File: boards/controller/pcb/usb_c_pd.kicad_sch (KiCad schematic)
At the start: 17 parts, among them J5001 699C124-2A6-111, U5001 USBLC6-2SC6, U5002 TCPP01-M12, U5003 ISZ065N03L5SATMA1

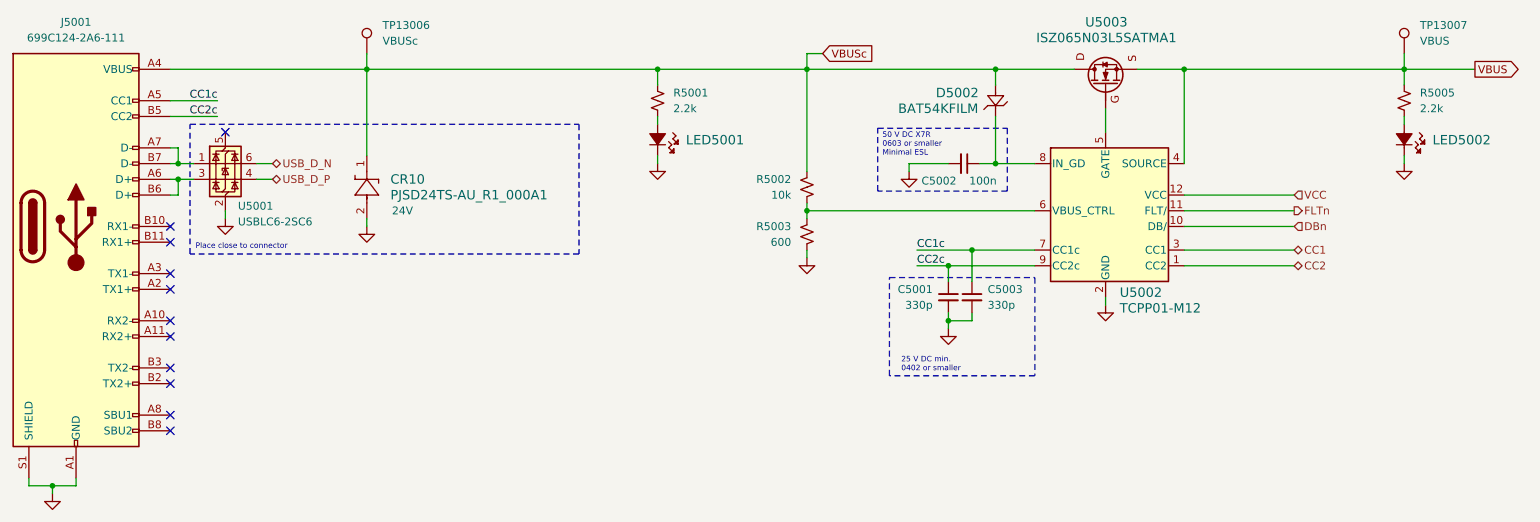
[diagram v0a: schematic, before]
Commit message: controller: pcb: Update schematic + layout
Signed-off-by: Nicholas Loehrke <nicholasnloehrke@gmail.com>
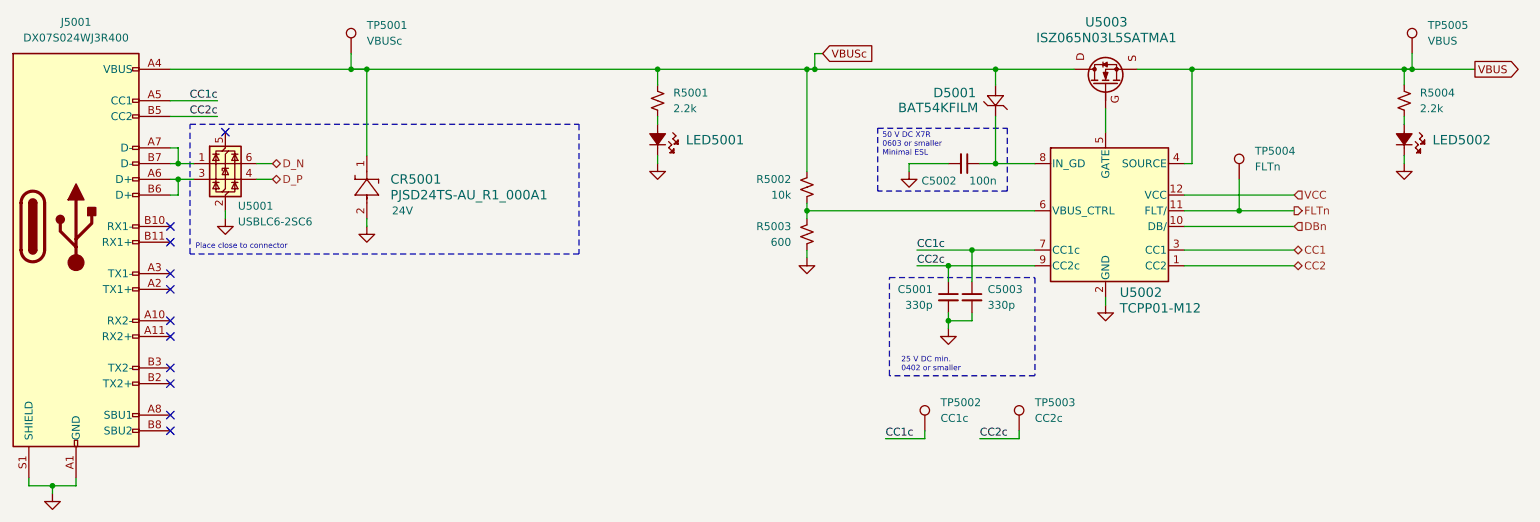
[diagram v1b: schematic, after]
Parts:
- removed D5002: BAT54KFILM, SOD-523_STM, symbol BAT54KFILM:BAT54KFILM
- removed J5001: 699C124-2A6-111, symbol Connector:USB_C_Receptacle
- added D5001: BAT54KFILM, BAT54KFILM:BAT54KFILM, symbol BAT54KFILM:BAT54KFILM
- added J5001: DX07S024WJ3R400, DX07S024WJ3R400:JAE_DX07S024WJ3R400, symbol DX07S024WJ3R400:DX07S024WJ3R400
- added TP5002: CC1c, TestPoint:TestPoint_Pad_D1.0mm, symbol Connector:TestPoint
- added TP5003: CC2c, TestPoint:TestPoint_Pad_D1.0mm, symbol Connector:TestPoint
- added TP5004: FLTn, TestPoint:TestPoint_Pad_D1.0mm, symbol Connector:TestPoint
- C5001, C5002, C5003: footprint (none) -> Capacitor_SMD:C_0402_1005Metric
- CR5001: renamed from CR10; footprint CR_SOD-523_PNJ -> PJSD24TS-AU_R1_000A1:PJSD24TS-AU_R1_000A1
- LED5001, LED5002: footprint LED_B1911PG--20D000514U1930_HVK -> B1911PG--20D000514U1930:B1911PG--20D000514U1930
- R5001: footprint (none) -> Resistor_SMD:R_0603_1608Metric
- R5002, R5003: footprint (none) -> Resistor_SMD:R_0402_1005Metric
- R5004: renamed from R5005; footprint (none) -> Resistor_SMD:R_0603_1608Metric
- TP5001: renamed from TP13006; footprint (none) -> TestPoint:TestPoint_Pad_D1.0mm
- TP5005: renamed from TP13007; footprint (none) -> TestPoint:TestPoint_Pad_D1.0mm
- U5002: footprint QFN12_TCPP01-M12_STM -> Package_DFN_QFN:QFN-12-1EP_3x3mm_P0.5mm_EP1.45x1.45mm
- U5003: footprint PG-TSDSON-8-25 -> ISZ065N03L5SATMA1:ISZ065N03L5SATMA1
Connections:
- net CC1c: now also J5001.A5 (CC1), TP5002.1
- net CC2c: now also J5001.B5 (CC2), TP5003.1
- net FLTn: now also TP5004.1
- net GND: now also J5001.A1 (GND), J5001.A12 (GND), J5001.B1 (GND), J5001.B12 (GND), J5001.S1 (SHIELD)
- net VBUSc: now also D5001.2, J5001.A4 (VBUS), J5001.A9 (VBUS), J5001.B4 (VBUS), J5001.B9 (VBUS)
- net at U5001.1 (I/O1): now also J5001.A7 (D-), J5001.B7 (D-)
- net at U5001.3 (I/O2): now also J5001.A6 (D+), J5001.B6 (D+)
- net at C5002.1, U5002.8 (IN_GD): now also D5001.1
- net USB_D_N renamed D_N
- net USB_D_P renamed D_P
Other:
- moved on the sheet: TP5001, TP5005

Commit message: controller: Update BOM
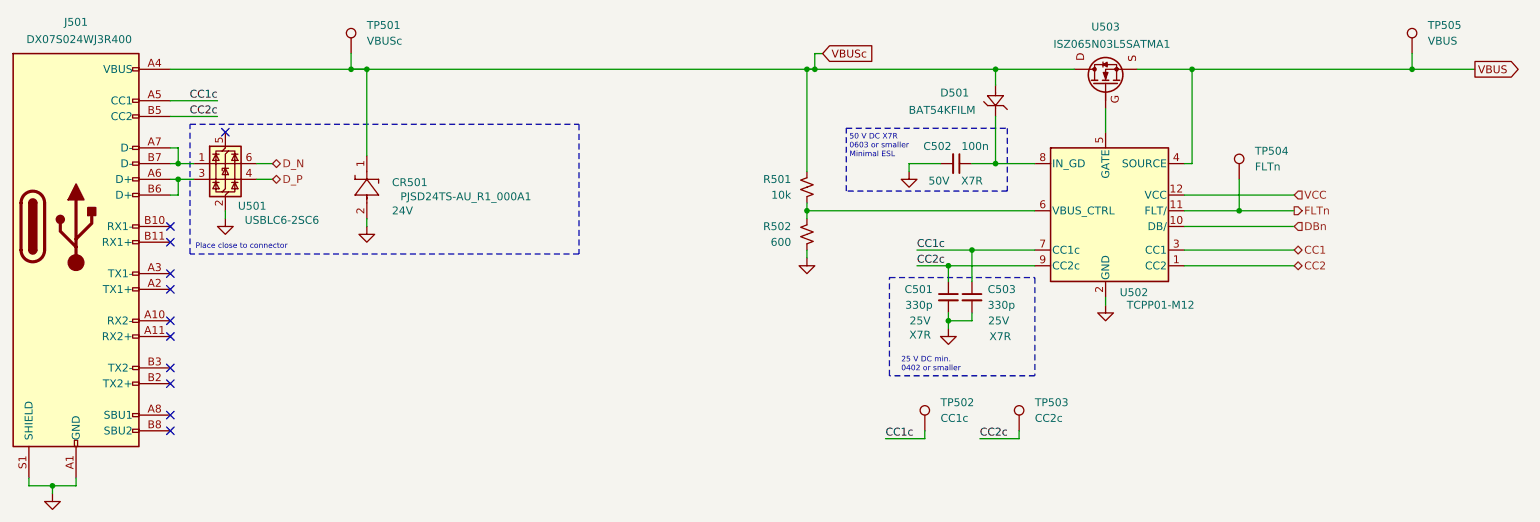
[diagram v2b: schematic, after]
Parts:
- removed LED5001, LED5002: B1911PG--20D000514U1930, B1911PG--20D000514U1930:B1911PG--20D000514U1930, symbol B1911PG--20D000514U1930:B1911PG--20D000514U1930
- removed R5001, R5004: 2.2k, Resistor_SMD:R_0603_1608Metric, symbol Device:R_Small_US
- C501: renamed from C5001; TCC (none) -> X7R; Voltage (none) -> 25V
- C502: renamed from C5002; TCC (none) -> X7R; Voltage (none) -> 50V
- C503: renamed from C5003; TCC (none) -> X7R; Voltage (none) -> 25V
- CR501: renamed from CR5001; MPN (none) -> PJSD24TS-AU_R1_000A1
- D501: renamed from D5001; MPN (none) -> BAT54KFILM
- J501: renamed from J5001; MPN (none) -> DX07S024WJ3R400
- U501: renamed from U5001; MPN (none) -> USBLC6-2SC6
- U502: renamed from U5002; MPN (none) -> TCPP01-M12
- U503: renamed from U5003; MPN (none) -> ISZ065N03L5SATMA1
- renumbered R5002 to R501, R5003 to R502, TP5001 to TP501, TP5002 to TP502, TP5003 to TP503, TP5004 to TP504, TP5005 to TP505
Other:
- moved on the sheet: C502
